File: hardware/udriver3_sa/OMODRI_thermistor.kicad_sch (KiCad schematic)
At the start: 9 parts, among them U16 OPA333xxDCK

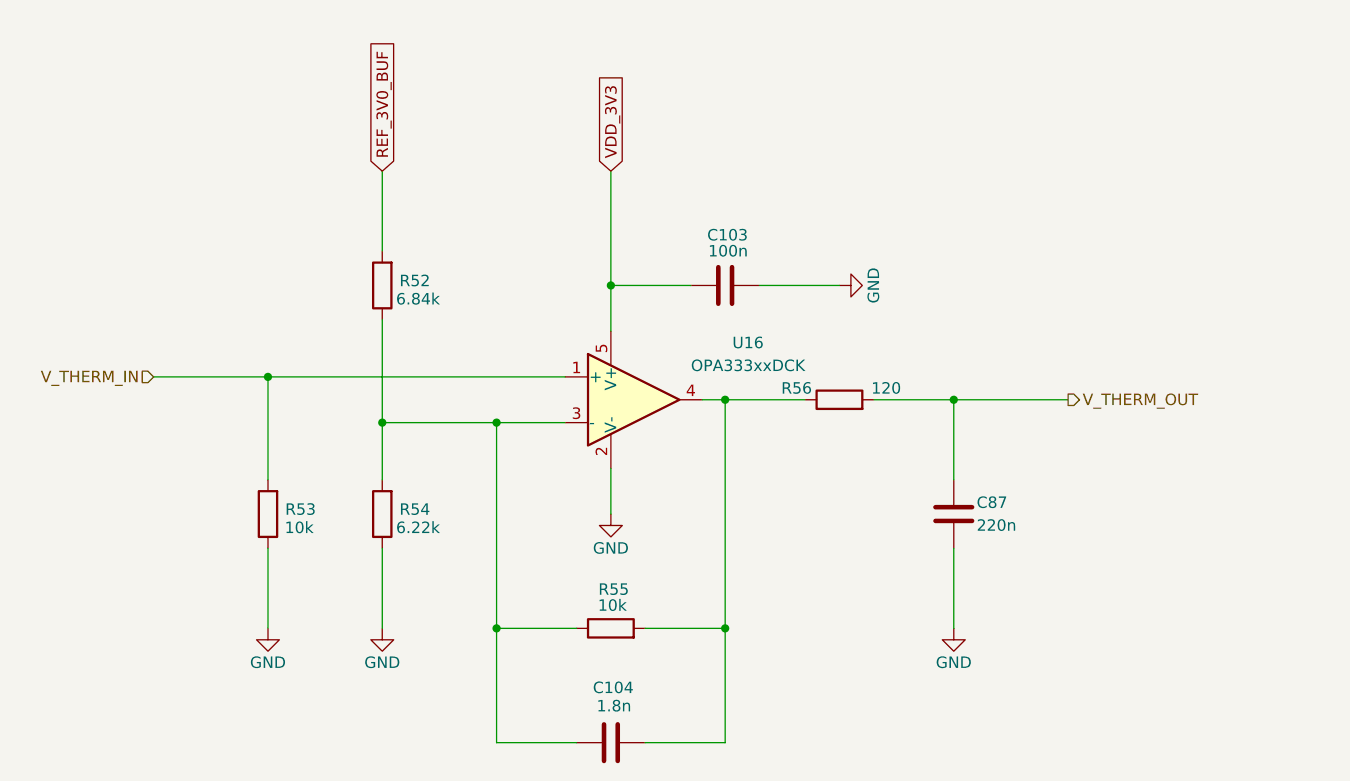
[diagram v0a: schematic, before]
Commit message: Third release of uOmodri Single Axis (uOmodri_SA). Add Test points.
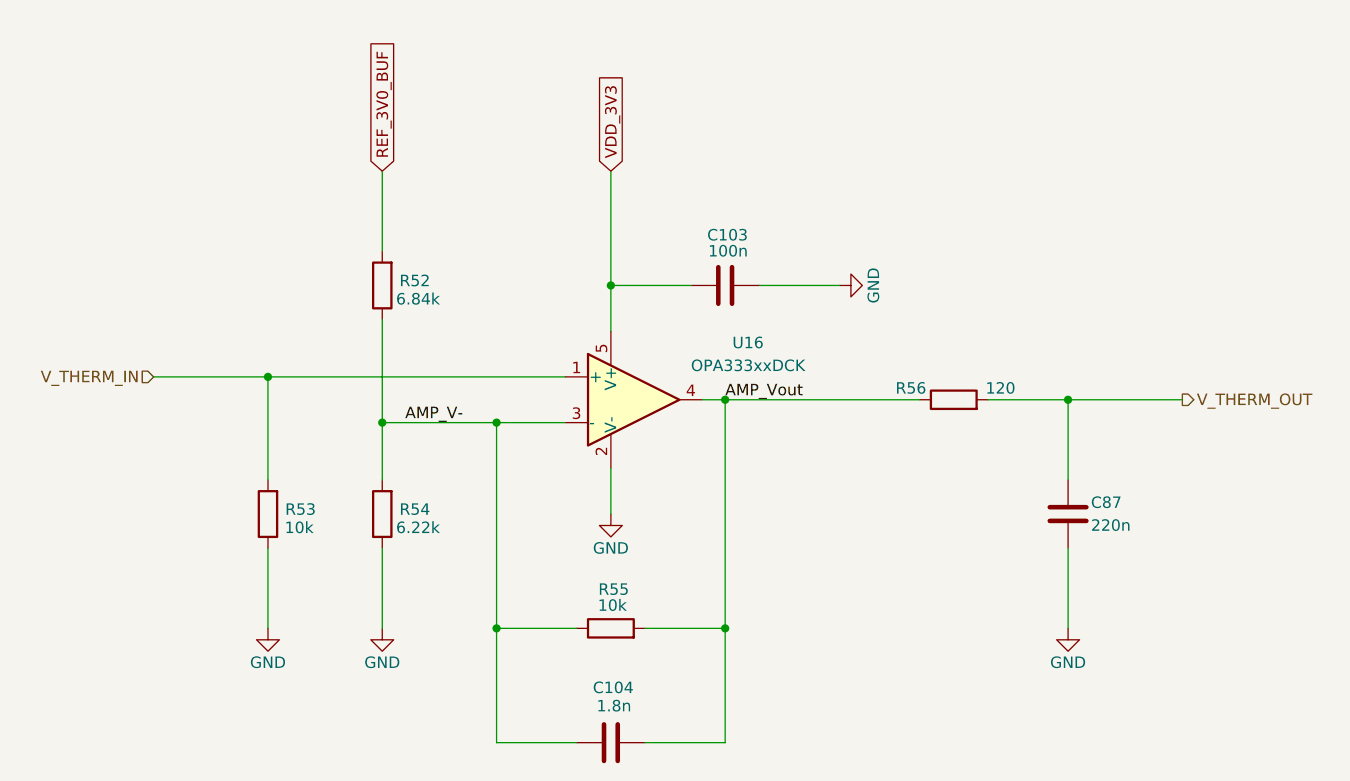
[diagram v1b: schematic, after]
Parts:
- U16: Assembling (none) -> SMD; DigiKey (none) -> 296-19547-1-ND; Farnell (none) -> 3117524; LCSC (none) -> C44193; Manufacturer (none) -> TEXAS INSTRUMENTS; Mouser (none) -> 595-OPA333AIDCKR; Part No (none) -> OPA333AIDCKR; RS (none) -> 660-9782
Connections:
- net AMP_V-: now reaches C104.1, R52.1, R54.2, R55.1, U16.3 (-)
- net AMP_Vout: now reaches C104.2, R55.2, R56.1, U16.4
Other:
- moved on the sheet: C87, R56
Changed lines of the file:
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@@
 	)
 	(junction
-		(at 165.1 101.6)
+		(at 177.8 101.6)
 		(diameter 0)
 		(color 0 0 0 0)
@@
 	(wire
 		(pts
-			(xy 156.21 101.6) (xy 165.1 101.6)
+			(xy 168.91 101.6) (xy 177.8 101.6)
 		)
 		(stroke
@@
 	(wire
 		(pts
-			(xy 139.7 101.6) (xy 148.59 101.6)
+			(xy 139.7 101.6) (xy 161.29 101.6)
 		)
 		(stroke
@@
 	(wire
 		(pts
-			(xy 165.1 101.6) (xy 177.8 101.6)
+			(xy 177.8 101.6) (xy 190.5 101.6)
 		)
 		(stroke
@@
 	(wire
 		(pts
-			(xy 165.1 101.6) (xy 165.1 110.49)
+			(xy 177.8 101.6) (xy 177.8 110.49)
 		)
 		(stroke
@@
 	(wire
 		(pts
-			(xy 165.1 118.11) (xy 165.1 127)
+			(xy 177.8 118.11) (xy 177.8 127)
 		)
 		(stroke
@@
 			(width 0)
 			(type default)
+		)
+	)
+	(label "AMP_V-"
+		(at 104.14 104.14 0)
+		(fields_autoplaced yes)
+		(effects
+			(font
+				(size 1.27 1.27)
+			)
+			(justify left bottom)
+		)
+	)
+	(label "AMP_Vout"
+		(at 139.7 101.6 0)
+		(fields_autoplaced yes)
+		(effects
+			(font
+				(size 1.27 1.27)
+			)
+			(justify left bottom)
 		)
 	)
@@
 	(hierarchical_label "V_THERM_OUT"
 		(shape output)
-		(at 177.8 101.6 0)
+		(at 190.5 101.6 0)
 		(fields_autoplaced yes)
 		(effects
@@
 	(symbol
 		(lib_id "Device:R")
-		(at 152.4 101.6 90)
+		(at 165.1 101.6 90)
 		(unit 1)
 		(exclude_from_sim no)
@@
 		(dnp no)
 		(property "Reference" "R56"
-			(at 149.352 100.33 90)
+			(at 162.052 100.33 90)
 			(effects
 				(font
@@
 		)
 		(property "Value" "120"
-			(at 159.258 100.33 90)
+			(at 171.958 100.33 90)
 			(effects
 				(font
@@
 		)
 		(property "Footprint" "Resistor_SMD:R_0201_0603Metric"
-			(at 152.4 103.378 90)
+			(at 165.1 103.378 90)
 			(effects
 				(font
@@
 		)
 		(property "Datasheet" "https://industrial.panasonic.com/sa/products/pt/general-purpose-chip-resistors/models/ERJ1GNF1200C"
-			(at 152.4 101.6 0)
+			(at 165.1 101.6 0)
 			(effects
 				(font
@@
 		)
 		(property "Description" "0201,120Ω, 0.05W, ±1%, SMD  resistor"
-			(at 152.4 101.6 0)
+			(at 165.1 101.6 0)
 			(effects
 				(font
@@
 		)
 		(property "DigiKey" "P122692CT-ND"
-			(at 152.4 101.6 0)
+			(at 165.1 101.6 0)
 			(effects
 				(font
@@
 		)
 		(property "Farnell" "2396857"
-			(at 152.4 101.6 0)
+			(at 165.1 101.6 0)
 			(effects
 				(font
@@
 		)
 		(property "Mouser" "667-ERJ-1GNF1200C"
-			(at 152.4 101.6 0)
+			(at 165.1 101.6 0)
 			(effects
 				(font
@@
 		)
 		(property "Part No" "ERJ1GNF1200C"
-			(at 152.4 101.6 0)
+			(at 165.1 101.6 0)
 			(effects
 				(font
@@
 		)
 		(property "RS" ""
-			(at 152.4 101.6 0)
+			(at 165.1 101.6 0)
 			(effects
 				(font
@@
 		)
 		(property "LCSC" "C278569"
-			(at 152.4 101.6 0)
+			(at 165.1 101.6 0)
 			(effects
 				(font
@@
 		)
 		(property "Manufacturer" "PANASONIC"
-			(at 152.4 101.6 0)
+			(at 165.1 101.6 0)
 			(effects
 				(font
@@
 		)
 		(property "Assembling" "SMD"
-			(at 152.4 101.6 0)
+			(at 165.1 101.6 0)
 			(effects
 				(font
@@
 	(symbol
 		(lib_id "power:GND")
-		(at 165.1 127 0)
+		(at 177.8 127 0)
 		(unit 1)
 		(exclude_from_sim no)
@@
 		(dnp no)
 		(property "Reference" "#PWR04"
-			(at 165.1 133.35 0)
+			(at 177.8 133.35 0)
 			(effects
 				(font
@@
 		)
 		(property "Value" "GND"
-			(at 165.1 130.81 0)
+			(at 177.8 130.81 0)
 			(effects
 				(font
@@
 		)
 		(property "Footprint" ""
-			(at 165.1 127 0)
+			(at 177.8 127 0)
 			(effects
 				(font
@@
 		)
 		(property "Datasheet" ""
-			(at 165.1 127 0)
+			(at 177.8 127 0)
 			(effects
 				(font
@@
 		)
 		(property "Description" "Power symbol creates a global label with name \"GND\" , ground"
-			(at 165.1 127 0)
+			(at 177.8 127 0)
 			(effects
 				(font
@@
 	(symbol
 		(lib_id "Device:C")
-		(at 165.1 114.3 0)
+		(at 177.8 114.3 0)
 		(unit 1)
 		(exclude_from_sim no)
@@
 		(dnp no)
 		(property "Reference" "C87"
-			(at 167.64 113.03 0)
+			(at 180.34 113.03 0)
 			(effects
 				(font
@@
 		)
 		(property "Value" "220n"
-			(at 167.64 115.57 0)
+			(at 180.34 115.57 0)
 			(effects
 				(font
@@
 		)
 		(property "Footprint" "Capacitor_SMD:C_0201_0603Metric"
-			(at 166.0652 118.11 0)
+			(at 178.7652 118.11 0)
 			(effects
 				(font
@@
 		)
 		(property "Datasheet" "https://www.murata.com/en-eu/products/productdetail?partno=GRM033R61C224KE14%23"
-			(at 165.1 114.3 0)
+			(at 177.8 114.3 0)
 			(effects
 				(font
@@
 		)
 		(property "Description" "0201, 220nf, 16V,  ±10%, X5R, SMD MLCC"
-			(at 165.1 114.3 0)
+			(at 177.8 114.3 0)
 			(effects
 				(font
@@
 		)
 		(property "DigiKey" "490-17040-1-ND"
-			(at 165.1 114.3 0)
+			(at 177.8 114.3 0)
 			(effects
 				(font
@@
 		)
 		(property "Farnell" "3582770"
-			(at 165.1 114.3 0)
+			(at 177.8 114.3 0)
 			(effects
 				(font
@@
 		)
 		(property "Mouser" "81-GRM033R61C224KE4D"
-			(at 165.1 114.3 0)
+			(at 177.8 114.3 0)
 			(effects
 				(font
@@
 		)
 		(property "Part No" "GRM033R61C224KE14D"
-			(at 165.1 114.3 0)
+			(at 177.8 114.3 0)
 			(effects
 				(font
@@
 		)
 		(property "RS" ""
-			(at 165.1 114.3 0)
+			(at 177.8 114.3 0)
 			(effects
 				(font
@@
 		)
 		(property "LCSC" "C161474"
-			(at 165.1 114.3 0)
+			(at 177.8 114.3 0)
 			(effects
 				(font
@@
 		)
 		(property "Manufacturer" "MURATA"
-			(at 165.1 114.3 0)
+			(at 177.8 114.3 0)
 			(effects
 				(font
@@
 		)
 		(property "Assembling" "SMD"
-			(at 165.1 114.3 0)
+			(at 177.8 114.3 0)
 			(effects
 				(font
@@
 			)
 		)
-		(property "Description" "Single 1.8V, microPower, CMOS Operational Amplifiers, Zero-Drift Series, SC-70-5"
+		(property "Description" "SC-70-5, Single 1.8V, microPower, CMOS Operational Amplifiers, Zero-Drift Series, SC-70-5"
 			(at 129.54 101.6 0)
 			(effects
+				(font
+					(size 1.27 1.27)
+				)
+				(hide yes)
+			)
+		)
+		(property "Manufacturer" "TEXAS INSTRUMENTS"
+			(at 129.54 101.6 0)
+			(effects
+				(font
+					(size 1.27 1.27)
+				)
+				(hide yes)
+			)
+		)
+		(property "DigiKey" "296-19547-1-ND"
+			(at 129.54 101.6 0)
+			(effects
+				(font
+					(size 1.27 1.27)
+				)
+				(hide yes)
+			)
+		)
+		(property "Farnell" "3117524"
+			(at 129.54 101.6 0)
+			(effects
+				(font
+					(size 1.27 1.27)
+				)
+				(hide yes)
+			)
+		)
+		(property "LCSC" "  C44193"
+			(at 129.54 101.6 0)
+			(effects
+				(font
+					(size 1.27 1.27)
+				)
+				(hide yes)
+			)
+		)
+		(property "Mouser" "595-OPA333AIDCKR"
+			(at 129.54 101.6 0)
+			(effects
+				(font
+					(size 1.27 1.27)
+				)
+				(hide yes)
+			)
+		)
+		(property "Part No" "OPA333AIDCKR"
+			(at 129.54 101.6 0)
+			(effects
+				(font
+					(size 1.27 1.27)
+				)
+				(hide yes)
+			)
+		)
+		(property "RS" "660-9782"
+			(at 129.54 101.6 0)
+			(effects
+				(font
+					(size 1.27 1.27)
+				)
+				(hide yes)
+			)
+		)
+		(property "Assembling" "SMD"
+			(at 129.54 101.6 0)
+			(effects

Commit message: Update on uOmodri_SA. Remove USB, com SPI & debug connectors for integration into Myactuator motors. Connectors replaced by a ZIF connector.
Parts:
- renumbered C103 to C102, C87 to C103, R52 to R50, R56 to R51, R53 to R52, R54 to R53, R55 to R54
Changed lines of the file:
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@@
 	(title_block
 		(title "Open MOtor DRiver Initiative  - Single Axis (OMODRI_SA)")
-		(date "2024-03-20")
+		(date "2024-11-08")
 		(rev "1.0")
 		(company "LAAS/CNRS")
@@
 		(on_board yes)
 		(dnp no)
-		(property "Reference" "R54"
+		(property "Reference" "R53"
 			(at 106.934 113.792 0)
 			(effects
@@
 			(project "omodri_sa_laas"
 				(path "/de5b13f0-933a-4c4d-9979-13dc57b13241/b535f441-e5f2-4a7b-a0a6-02c4bb8f1fa2"
-					(reference "R54")
+					(reference "R53")
 					(unit 1)
 				)
@@
 		(on_board yes)
 		(dnp no)
-		(property "Reference" "#PWR0167"
+		(property "Reference" "#PWR0151"
 			(at 158.75 88.9 0)
 			(effects
@@
 			(project "omodri_sa_laas"
 				(path "/de5b13f0-933a-4c4d-9979-13dc57b13241/b535f441-e5f2-4a7b-a0a6-02c4bb8f1fa2"
-					(reference "#PWR0167")
+					(reference "#PWR0151")
 					(unit 1)
 				)
@@
 		(on_board yes)
 		(dnp no)
-		(property "Reference" "R55"
+		(property "Reference" "R54"
 			(at 129.032 122.682 90)
 			(effects
@@
 			(project "omodri_sa_laas"
 				(path "/de5b13f0-933a-4c4d-9979-13dc57b13241/b535f441-e5f2-4a7b-a0a6-02c4bb8f1fa2"
-					(reference "R55")
+					(reference "R54")
 					(unit 1)
 				)
@@
 		(on_board yes)
 		(dnp no)
-		(property "Reference" "R56"
+		(property "Reference" "R51"
 			(at 162.052 100.33 90)
 			(effects
@@
 			(project "omodri_sa_laas"
 				(path "/de5b13f0-933a-4c4d-9979-13dc57b13241/b535f441-e5f2-4a7b-a0a6-02c4bb8f1fa2"
-					(reference "R56")
+					(reference "R51")
 					(unit 1)
 				)
@@
 		(on_board yes)
 		(dnp no)
-		(property "Reference" "#PWR04"
+		(property "Reference" "#PWR0155"
 			(at 177.8 133.35 0)
 			(effects
@@
 			(project "omodri_sa_laas"
 				(path "/de5b13f0-933a-4c4d-9979-13dc57b13241/b535f441-e5f2-4a7b-a0a6-02c4bb8f1fa2"
-					(reference "#PWR04")
+					(reference "#PWR0155")
 					(unit 1)
 				)
@@
 		(on_board yes)
 		(dnp no)
-		(property "Reference" "C103"
+		(property "Reference" "C102"
 			(at 142.24 83.312 90)
 			(effects
@@
 			(project "omodri_sa_laas"
 				(path "/de5b13f0-933a-4c4d-9979-13dc57b13241/b535f441-e5f2-4a7b-a0a6-02c4bb8f1fa2"
-					(reference "C103")
+					(reference "C102")
 					(unit 1)
 				)
@@
 		(on_board yes)
 		(dnp no)
-		(property "Reference" "R52"
+		(property "Reference" "R50"
 			(at 106.934 88.392 0)
 			(effects
@@
 			(project "omodri_sa_laas"
 				(path "/de5b13f0-933a-4c4d-9979-13dc57b13241/b535f441-e5f2-4a7b-a0a6-02c4bb8f1fa2"
-					(reference "R52")
+					(reference "R50")
 					(unit 1)
 				)
@@
 		(on_board yes)
 		(dnp no)
-		(property "Reference" "#PWR0168"
+		(property "Reference" "#PWR0152"
 			(at 127 120.65 0)
 			(effects
@@
 			(project "omodri_sa_laas"
 				(path "/de5b13f0-933a-4c4d-9979-13dc57b13241/b535f441-e5f2-4a7b-a0a6-02c4bb8f1fa2"
-					(reference "#PWR0168")
+					(reference "#PWR0152")
 					(unit 1)
 				)
@@
 		(on_board yes)
 		(dnp no)
-		(property "Reference" "R53"
+		(property "Reference" "R52"
 			(at 94.234 113.792 0)
 			(effects
@@
 			(project "omodri_sa_laas"
 				(path "/de5b13f0-933a-4c4d-9979-13dc57b13241/b535f441-e5f2-4a7b-a0a6-02c4bb8f1fa2"
-					(reference "R53")
+					(reference "R52")
 					(unit 1)
 				)
@@
 		(on_board yes)
 		(dnp no)
-		(property "Reference" "#PWR0171"
+		(property "Reference" "#PWR0154"
 			(at 101.6 133.35 0)
 			(effects
@@
 			(project "omodri_sa_laas"
 				(path "/de5b13f0-933a-4c4d-9979-13dc57b13241/b535f441-e5f2-4a7b-a0a6-02c4bb8f1fa2"
-					(reference "#PWR0171")
+					(reference "#PWR0154")
 					(unit 1)
 				)
@@
 		(on_board yes)
 		(dnp no)
-		(property "Reference" "C87"
+		(property "Reference" "C103"
 			(at 180.34 113.03 0)
 			(effects
@@
 			(project "omodri_sa_laas"
 				(path "/de5b13f0-933a-4c4d-9979-13dc57b13241/b535f441-e5f2-4a7b-a0a6-02c4bb8f1fa2"
-					(reference "C87")
+					(reference "C103")
 					(unit 1)
 				)
@@
 		(on_board yes)
 		(dnp no)
-		(property "Reference" "#PWR0170"
+		(property "Reference" "#PWR0153"
 			(at 88.9 133.35 0)
 			(effects
@@
 			(project "omodri_sa_laas"
 				(path "/de5b13f0-933a-4c4d-9979-13dc57b13241/b535f441-e5f2-4a7b-a0a6-02c4bb8f1fa2"
-					(reference "#PWR0170")
+					(reference "#PWR0153")
 					(unit 1)
 				)
